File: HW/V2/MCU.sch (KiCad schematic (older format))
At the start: 29 parts, among them J3 USB_B_Mini, SW1 SW_Push, U10 74HCT2G14GV, U11 OLED_128x64_i2c_0.96\", U14 OLED_128x64_SPI_0.96\", U3 Bluepill, U8 CH340G, U9 M24C01-WMN, Y1 12MHZ

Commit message: V2 milling and BOM
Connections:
- net powerTemp: no longer names the net of U3.13 (PB0_ADC8_PWM)
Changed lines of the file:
@@
 Text HLabel 6700 3050 2    50   Input ~ 0
 MOSFETtemp
-Text HLabel 6700 3150 2    50   Input ~ 0
-powerTemp
 $Comp
 L Peters:OLED_128x64_i2c_0.96" U11

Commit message: BOM
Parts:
- added J?: I2CHeader, symbol Connector:Conn_01x04_Male
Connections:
- net GND: now also J?.1 (Pin_1)
- net SDA: now also J?.2 (Pin_2), J?.3 (Pin_3)
- net VCC: now also J?.4 (Pin_4)
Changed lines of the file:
@@
 	-1   0    0    1
 $EndComp
+$Comp
+L Connector:Conn_01x04_Male J?
+U 1 1 5C62E9D6
+P 4550 1550
+F 0 "J?" V 4610 1691 50  0000 L CNN
+F 1 "I2CHeader" V 4701 1691 50  0000 L CNN
+F 2 "" H 4550 1550 50  0001 C CNN
+F 3 "~" H 4550 1550 50  0001 C CNN
+	1    4550 1550
+	0    1    1    0
+$EndComp
+Text HLabel 4450 1750 3    50   Input ~ 0
+SDA
+Text HLabel 4550 1750 3    50   Input ~ 0
+SDA
+$Comp
+L power:VCC #PWR?
+U 1 1 5C630BDC
+P 4350 1750
+F 0 "#PWR?" H 4350 1600 50  0001 C CNN
+F 1 "VCC" H 4367 1923 50  0000 C CNN
+F 2 "" H 4350 1750 50  0001 C CNN
+F 3 "" H 4350 1750 50  0001 C CNN
+	1    4350 1750
+	-1   0    0    1
+$EndComp
+$Comp
+L power:GND #PWR?
+U 1 1 5C630C5F
+P 4650 1750
+F 0 "#PWR?" H 4650 1500 50  0001 C CNN
+F 1 "GND" H 4800 1700 50  0000 C CNN
+F 2 "" H 4650 1750 50  0001 C CNN
+F 3 "" H 4650 1750 50  0001 C CNN
+	1    4650 1750
+	1    0    0    -1
+$EndComp
 $EndSCHEMATC

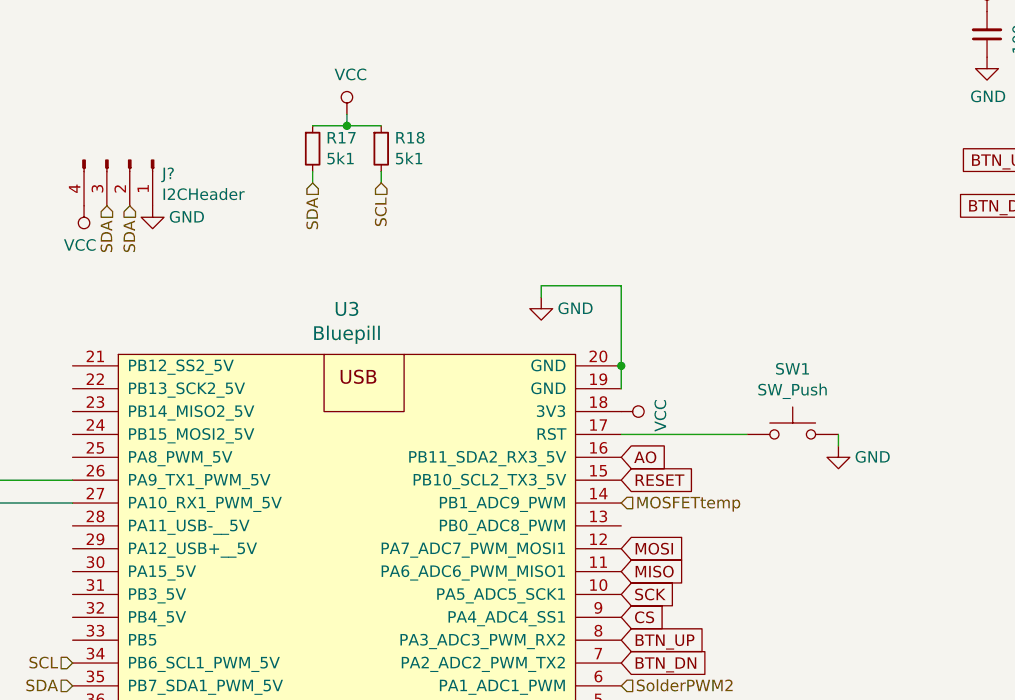
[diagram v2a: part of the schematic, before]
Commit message: piggyback ADC amp
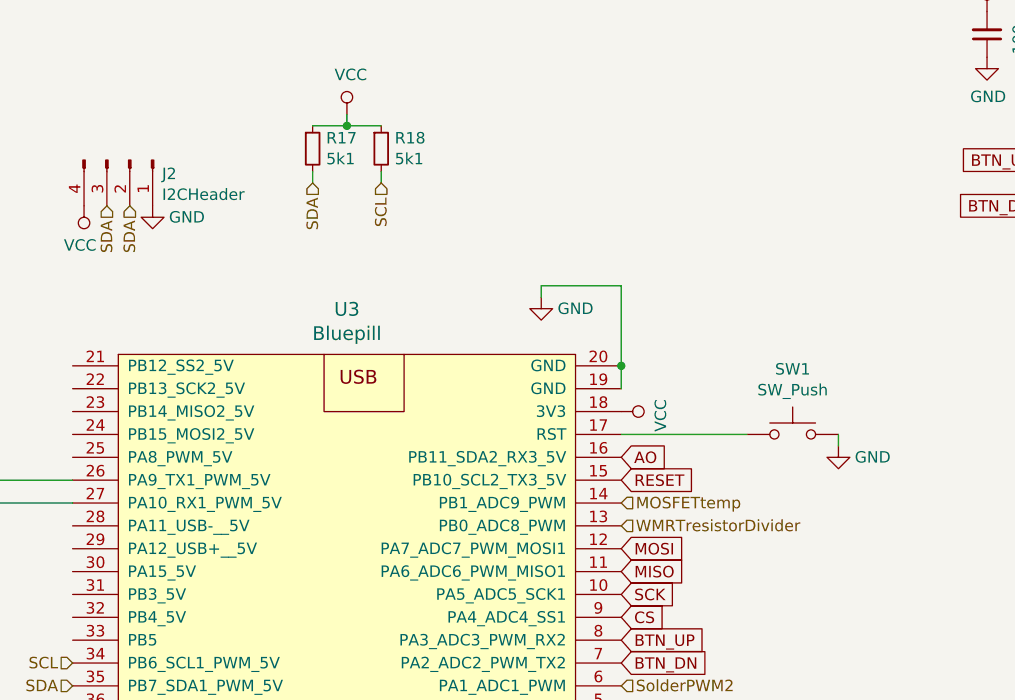
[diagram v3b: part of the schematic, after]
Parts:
- J2: renamed from J?; footprint (none) -> Connector_PinSocket_2.54mm:PinSocket_1x04_P2.54mm_Vertical
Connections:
- net WMRTresistorDivider: now reaches U3.13 (PB0_ADC8_PWM)
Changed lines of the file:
@@
 $EndComp
 $Comp
-L Connector:Conn_01x04_Male J?
+L Connector:Conn_01x04_Male J2
 U 1 1 5C62E9D6
 P 4550 1550
-F 0 "J?" V 4610 1691 50  0000 L CNN
+F 0 "J2" V 4610 1691 50  0000 L CNN
 F 1 "I2CHeader" V 4701 1691 50  0000 L CNN
-F 2 "" H 4550 1550 50  0001 C CNN
+F 2 "Connector_PinSocket_2.54mm:PinSocket_1x04_P2.54mm_Vertical" H 4550 1550 50  0001 C CNN
 F 3 "~" H 4550 1550 50  0001 C CNN
 	1    4550 1550
@@
 SDA
 $Comp
-L power:VCC #PWR?
+L power:VCC #PWR0130
 U 1 1 5C630BDC
 P 4350 1750
-F 0 "#PWR?" H 4350 1600 50  0001 C CNN
+F 0 "#PWR0130" H 4350 1600 50  0001 C CNN
 F 1 "VCC" H 4367 1923 50  0000 C CNN
 F 2 "" H 4350 1750 50  0001 C CNN
@@
 $EndComp
 $Comp
-L power:GND #PWR?
+L power:GND #PWR0131
 U 1 1 5C630C5F
 P 4650 1750
-F 0 "#PWR?" H 4650 1500 50  0001 C CNN
+F 0 "#PWR0131" H 4650 1500 50  0001 C CNN
 F 1 "GND" H 4800 1700 50  0000 C CNN
 F 2 "" H 4650 1750 50  0001 C CNN
@@
 	1    0    0    -1
 $EndComp
+Text HLabel 6700 3150 2    50   Input ~ 0
+WMRTresistorDivider
 $EndSCHEMATC
